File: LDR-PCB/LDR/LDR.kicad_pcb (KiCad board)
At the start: 2 copper layers, 22.6 x 20.4 mm, 9 parts, among them J1 Conn_01x03_Socket, Q1 NPN, U1 type="X" model="OPAMP" lib=""

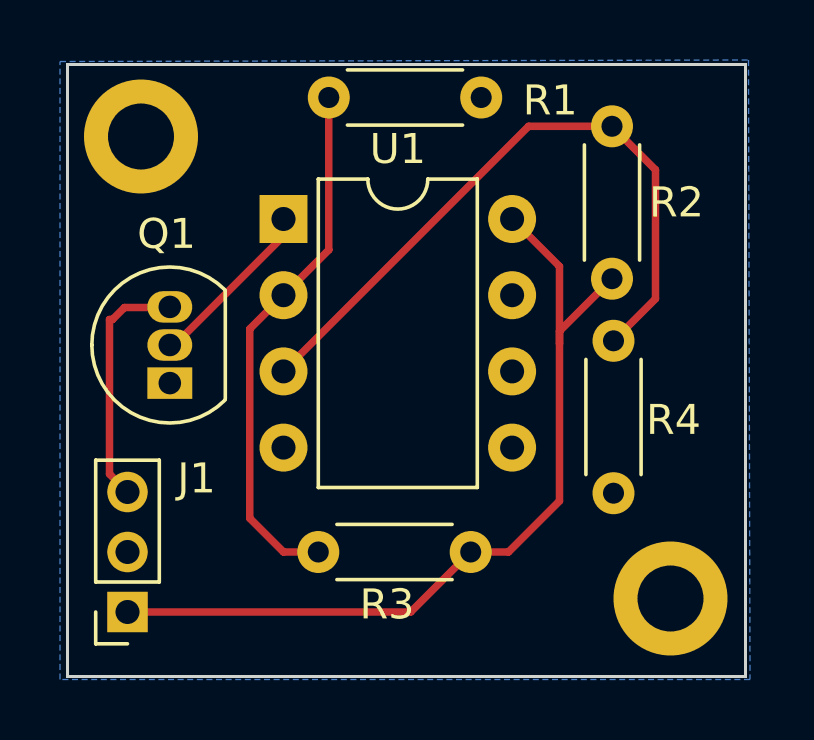
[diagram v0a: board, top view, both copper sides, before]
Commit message: LDR schakeling update naar LM311P
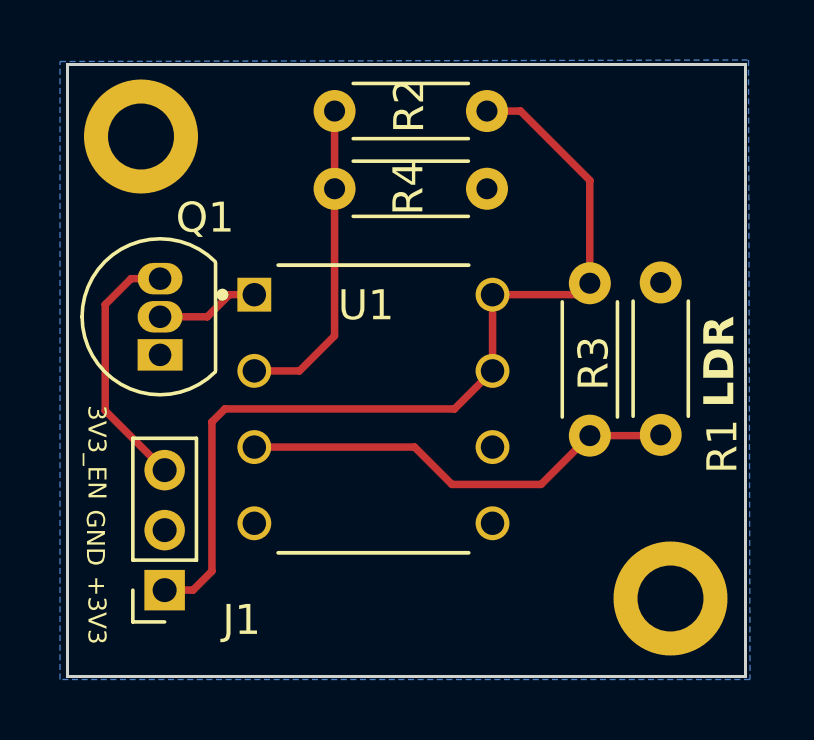
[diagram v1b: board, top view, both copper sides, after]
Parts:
- R2, R3: value R -> 2K2
- R4: value R -> 1K8
- U1: value type="X" model="OPAMP" lib="" -> LM311P; footprint Package_DIP:DIP-8_W7.62mm -> LM311P:DIP794W45P254L959H508Q8
- moved R1 15.8 mm to (220.6, 64.8), turned to 90 degrees
- moved R4 10.6 mm to (209.7, 56.6), turned to 0 degrees
- moved R3 9.80 mm to (218.2, 59.8), turned to -90 degrees
- moved U1 7.01 mm to (211.0, 64.0)
- moved R2 6.97 mm to (214.8, 54.1), turned to 180 degrees
- moved J1 1.44 mm to (204.0, 70.0)
- moved Q1 1.00 mm to (203.9, 62.2)
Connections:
- R1 pad 1: Net-(U1--A) -> Net-(U1-IN-)
- R2 pad 2: Net-(U1-+A) -> Net-(U1-IN+)
- R3 pad 2: Net-(U1--A) -> Net-(U1-IN-)
- R4 pad 1: Net-(U1-+A) -> Net-(U1-IN+)
- U1 pad 2: Net-(U1--A) -> Net-(U1-IN+)
- U1 pad 3: Net-(U1-+A) -> Net-(U1-IN-)
- U1 pad 5: (no net) -> unconnected-(U1-BALANCE-Pad5)
- U1 pad 6: (no net) -> unconnected-(U1-BAL/STRB-Pad6)
- U1 pad 7: (no net) -> +3V3
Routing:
- net Net-(U1-+A): track 22.7 -> 0.00 mm
- net Net-(U1--A): track 17.9 -> 0.00 mm
- net Net-(U1-IN-): track 0.00 -> 14.7 mm
- net Net-(U1-IN+): track 0.00 -> 10.7 mm
- net +3V3: track 28.9 -> 30.6 mm
- net Net-(Q1-B): track 5.86 -> 4.29 mm
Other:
- board text added: "+3V3"
- board text added: "3V3_EN"
- board text added: "GND"
- board text added: "LDR"

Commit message: LDR connector, silkscreen AC,  Mounting hole main pcb aangepast
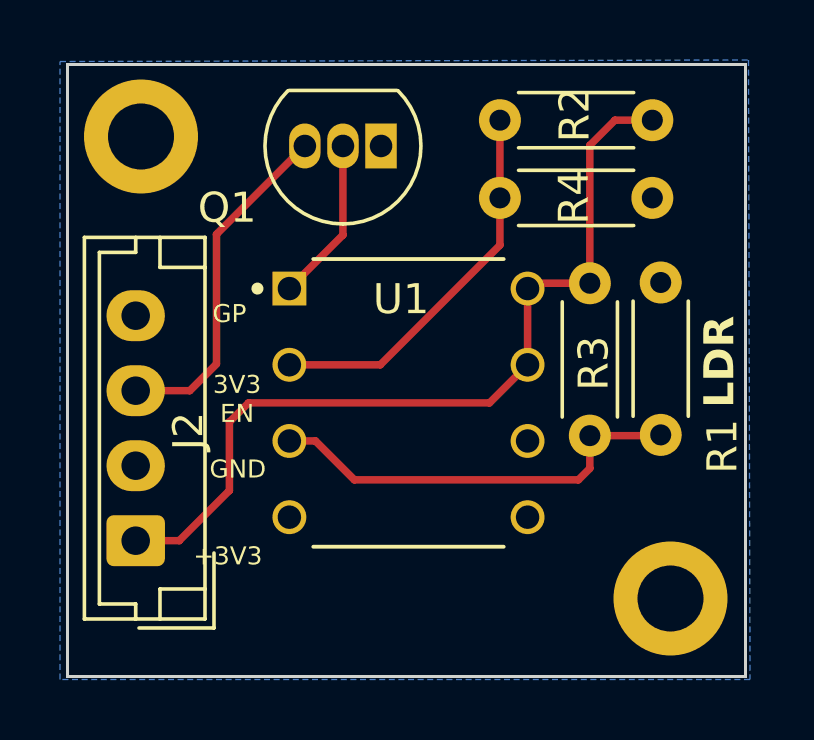
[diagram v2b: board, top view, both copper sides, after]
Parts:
- removed J1: Conn_01x03_Socket, Connector_PinSocket_2.00mm:PinSocket_1x03_P2.00mm_Vertical
- added J2: Conn_01x04_Socket, Connector_JST:JST_EH_B4B-EH-A_1x04_P2.50mm_Vertical, F.Cu at (203.1, 68.4)
- moved Q1 10.1 mm to (211.3, 55.2), turned to 180 degrees
- moved R2 5.52 mm to (220.3, 54.4)
- moved R4 5.52 mm to (215.2, 56.9)
- moved U1 1.19 mm to (212.2, 63.8)
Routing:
- net 3V3_en: track 8.53 -> 11.5 mm
- net Net-(U1-IN+): track 10.7 -> 12.8 mm
- net +3V3: track 30.6 -> 29.1 mm
- net Net-(Q1-B): track 4.29 -> 5.49 mm
- net Net-(U1-IN-): track 14.7 -> 14.2 mm
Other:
- board text added: "3V3 EN"
- board text added: "GP"
- board text removed: "3V3_EN"

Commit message: PCB aangepast naar specificaties van JLCpcb  en bestellen
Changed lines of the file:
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@@
       (drillshape 0)
       (scaleselection 1)
-      (outputdirectory "../gerber LDR pcb/")
+      (outputdirectory "../Gerber LDR pcb1.1/")
     )
   )
@@
     (fp_line (start 10 2.2) (end 10 -1.6)
       (stroke (width 0.1) (type solid)) (layer "F.Fab"))
-    (pad "1" thru_hole roundrect (at 0 0 90) (size 1.7 1.95) (drill 0.95) (layers "*.Cu" "*.Mask") (roundrect_rratio 0.147059)
+    (pad "1" thru_hole roundrect (at 0 0 90) (size 1.7 1.95) (drill 0.95) (layers "*.Cu" "*.Mask") (roundrect_rratio 0.1470588235)
       (net 3 "+3V3") (pinfunction "Pin_1") (pintype "passive"))
     (pad "2" thru_hole oval (at 2.5 0 90) (size 1.7 1.95) (drill 0.95) (layers "*.Cu" "*.Mask")
